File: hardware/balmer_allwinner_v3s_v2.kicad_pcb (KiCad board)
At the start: 4 copper layers, 60 x 60 mm, 118 parts, among them J1 JAE_SIM_Card_SF72S006, J11 Micro_SD_Card_Ebay, J2 UART, J3 Bus_PCI_Express_Mini, J4 USB_C_Receptacle, J8 HR911105_RJ45, SW1 SW_MEC_5G, SW2 SW_MEC_5G, U1 AllwinnerV3S, U10 TLV62568DBV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

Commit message: Small updates
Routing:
- net UART0_RX: track 56.4 -> 59.7 mm
- net UART0_TX: track 52.6 -> 55.0 mm
- net SPI_MISO: track 52.7 -> 53.3 mm

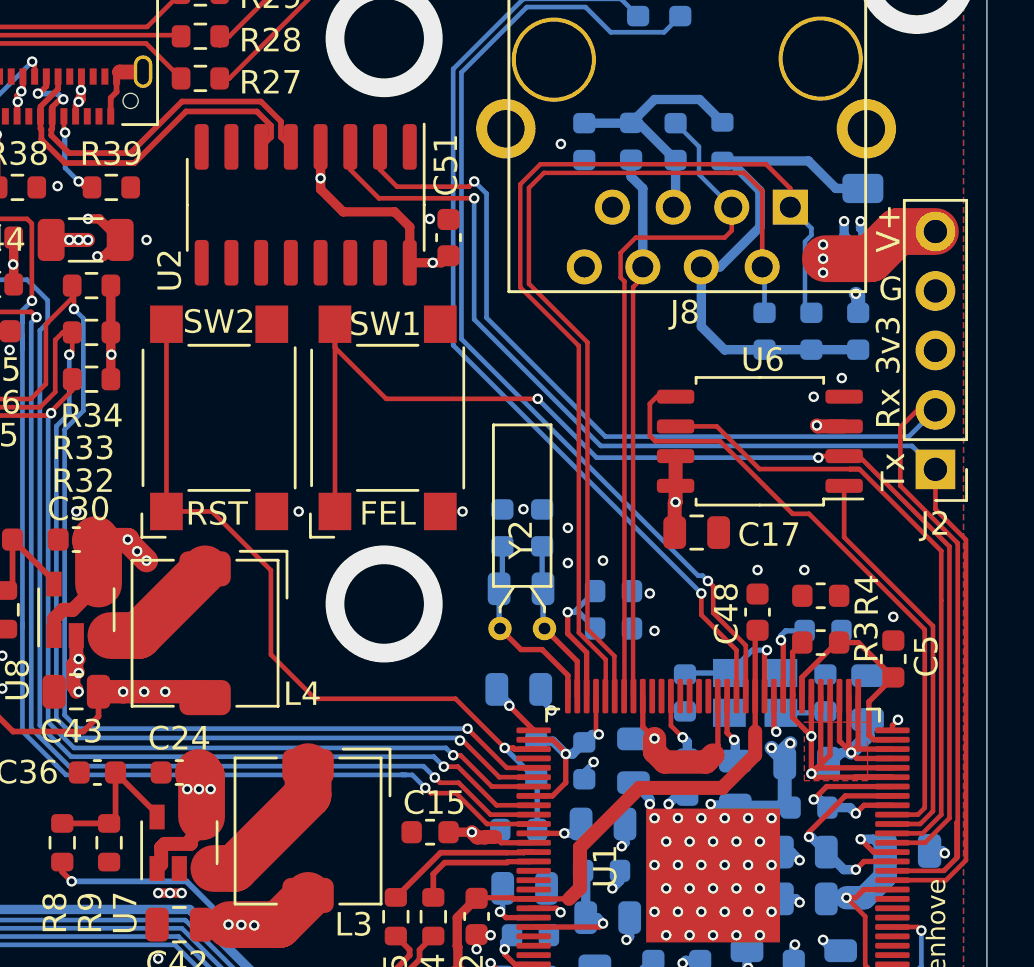
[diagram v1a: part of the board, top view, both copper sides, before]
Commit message: Removed FEL button
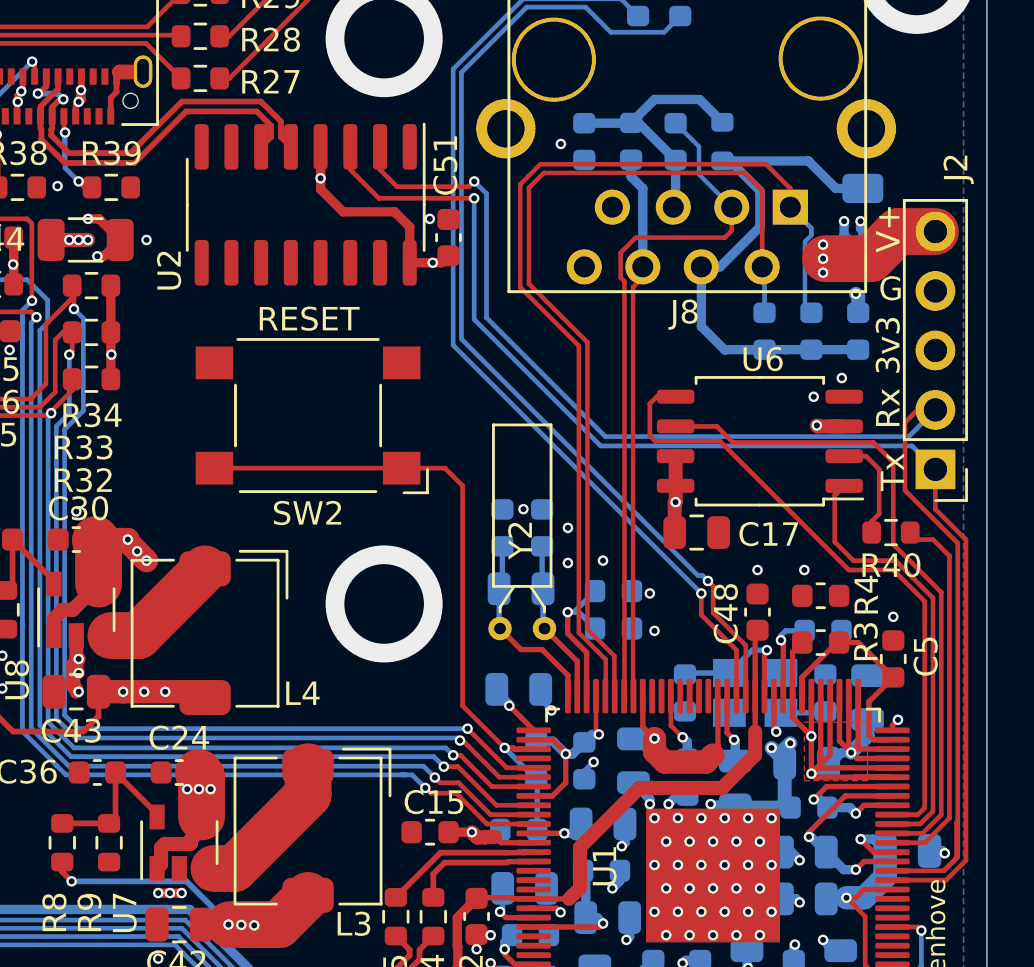
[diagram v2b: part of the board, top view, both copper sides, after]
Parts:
- removed SW1: SW_MEC_5G, Button_Switch_SMD:SW_SPST_Omron_B3FS-100xP
- added R40: 0R, Resistor_SMD:R_0603_1608Metric, F.Cu at (117.9, 101.8)
- moved SW2 3.80 mm to (93.0, 96.8), turned to 180 degrees
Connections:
- U6 pad 2: SPI_MISO -> Net-(R40-Pad2)
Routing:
- net SPI_MISO: track 53.3 -> 16.0 mm, vias 2 -> 0
- net RESET: track 34.1 -> 28.2 mm
- net Net-(R40-Pad2): track 0.00 -> 5.20 mm
- net SPI_CS: track 17.4 -> 18.8 mm
- net SPI_MOSI: track 26.9 -> 27.6 mm
- net SPI_SCK: track 27.6 -> 28.3 mm
- net GND: vias 148 -> 146
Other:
- board text added: "RESET"
- board text removed: "FEL"
- board text removed: "RST"

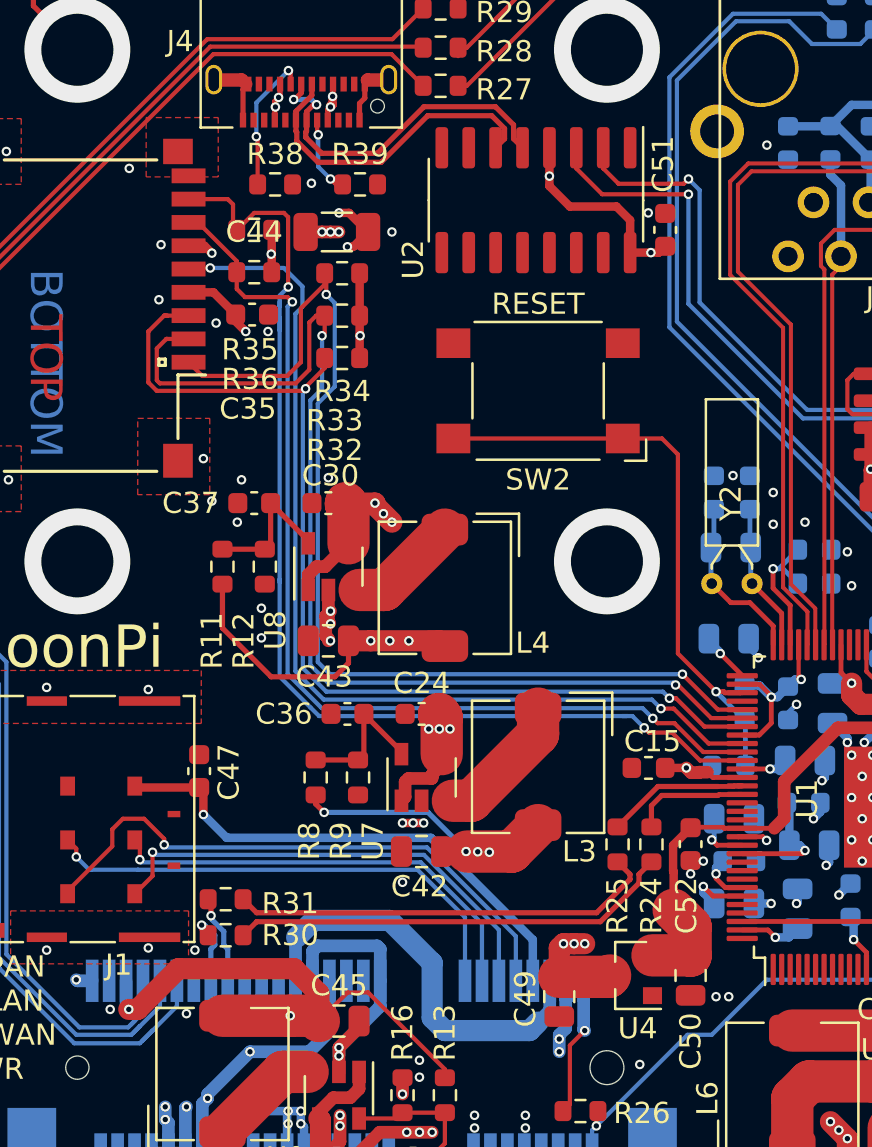
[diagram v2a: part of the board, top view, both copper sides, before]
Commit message: Removed USB series resistors on mPCIe side
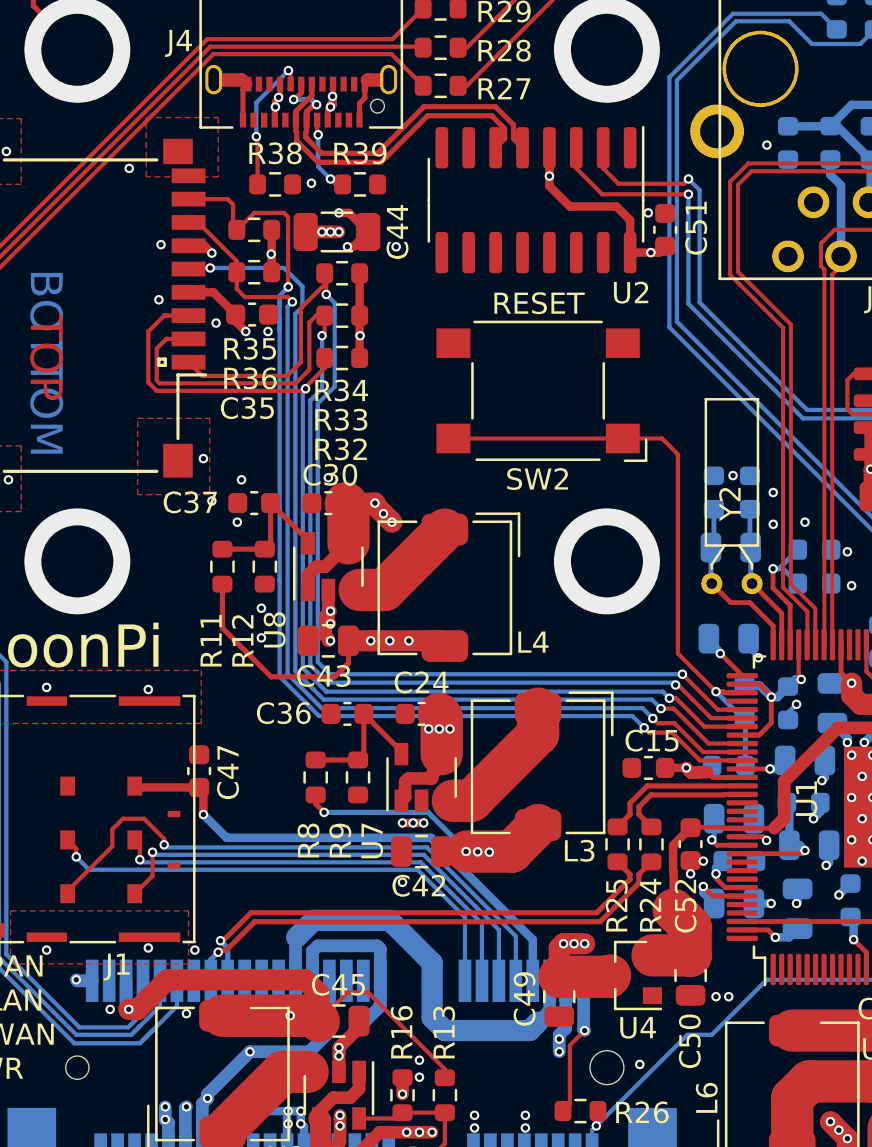
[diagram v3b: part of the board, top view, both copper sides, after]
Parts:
- removed R30, R31: 33, Resistor_SMD:R_0603_1608Metric
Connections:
- J3 pad 36: /Periphery/USB_H-D- -> USB-D-
- J3 pad 38: /Periphery/USB_H-D+ -> USB-D+
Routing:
- net /Periphery/USB_H-D-: track 4.26 -> 0.00 mm, vias 1 -> 0
- net /Periphery/USB_H-D+: track 3.76 -> 0.00 mm, vias 1 -> 0
- net USB-D-: track 20.3 -> 23.6 mm, vias 0 -> 1
- net USB-D+: track 21.0 -> 24.0 mm, vias 0 -> 1
- net /USB_D-D+: track 5.51 -> 6.31 mm

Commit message: Fixed DRC
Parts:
- moved C47 1.10 mm to (78.1, 114.8)
- moved R27 0.60 mm to (89.0, 82.4)
- moved R28 0.60 mm to (89.0, 80.6)
- moved R29 0.60 mm to (89.0, 78.8)
- moved C35 0.50 mm to (79.5, 93.7)
- moved J11 0.50 mm to (66.0, 93.8)
- moved R32 0.50 mm to (83.8, 95.8)
- moved R33 0.50 mm to (83.8, 93.8)
- moved R34 0.50 mm to (83.8, 91.8)
- moved R35 0.50 mm to (79.6, 89.7)
- moved R36 0.50 mm to (79.6, 91.7)
- moved C24 0.40 mm to (87.1, 112.0)
- moved C36 0.40 mm to (83.6, 112.0)
- moved C42 0.40 mm to (87.1, 118.5)
- moved J8 0.40 mm to (108.8, 81.3)
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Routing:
- net GND: track 88.0 -> 93.5 mm
- net VCC: track 176.6 -> 179.2 mm, vias 27 -> 29
- net Net-(C33-Pad1): track 23.8 -> 25.2 mm
- net EPHY-RXP: track 29.7 -> 30.7 mm
- net Net-(J3-Pad44): track 76.0 -> 77.0 mm
- net Net-(C47-Pad1): track 24.4 -> 25.2 mm
- net SDC0_D2: track 50.6 -> 50.0 mm
- net Net-(J3-Pad46): track 71.9 -> 72.5 mm
- net Net-(J3-Pad42): track 76.0 -> 76.6 mm
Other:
- net class Default: clearance 0.1524 -> 0.127
- net class Power: clearance 0.1524 -> 0.127
- rule trace_clearance: 0.1524 -> 0.127
- rule trace_min: 0.1016 -> 0.1778

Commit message: Rotated SIM
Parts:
- moved C47 5.38 mm to (77.9, 120.1), turned to 270 degrees
- moved J1 4.89 mm to (67.3, 115.5), turned to 90 degrees
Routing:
- net GND: track 93.5 -> 122.5 mm, vias 146 -> 139
- net Net-(C47-Pad1): track 25.2 -> 35.5 mm
- net Net-(J1-PadC3): track 22.7 -> 32.9 mm
- net Net-(J1-PadC2): track 21.2 -> 31.0 mm
- net Net-(J1-PadC6): track 23.5 -> 27.2 mm
- net Net-(J1-PadC7): track 27.9 -> 30.3 mm

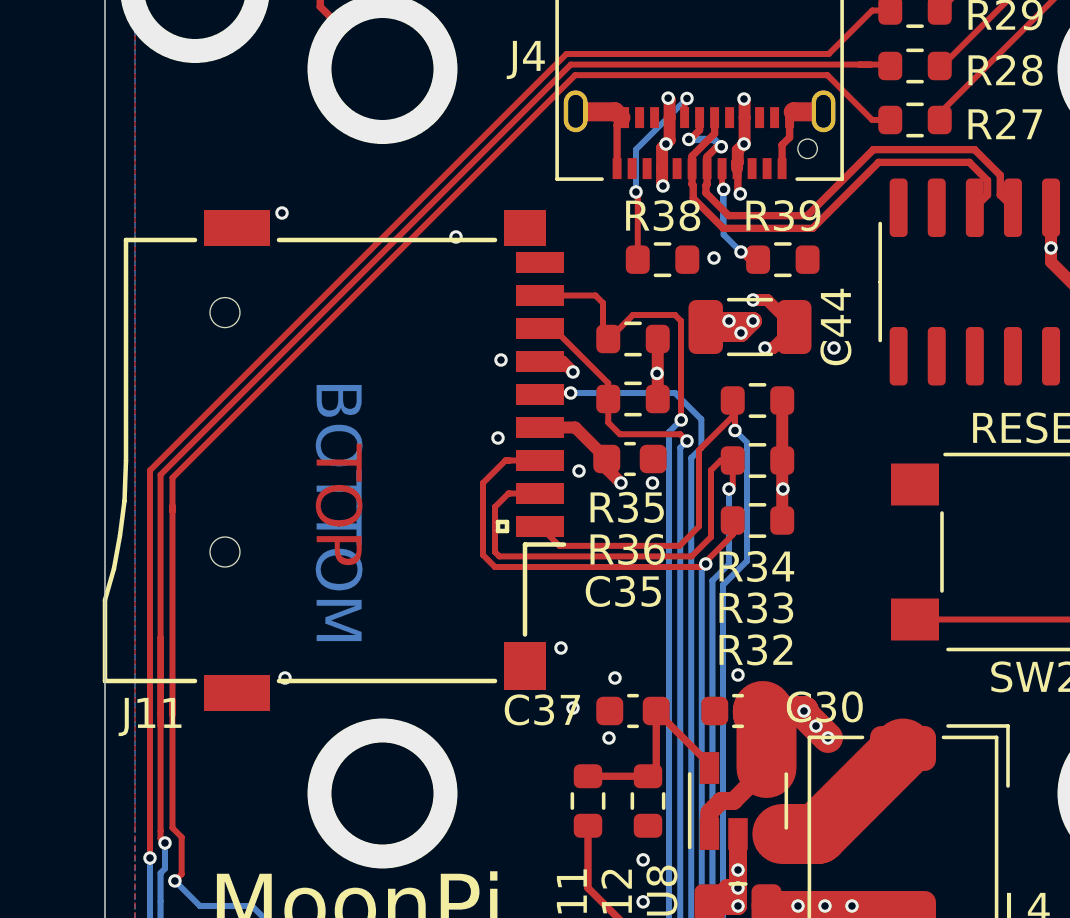
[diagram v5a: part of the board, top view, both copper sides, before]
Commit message: 0R between VBus and VCC
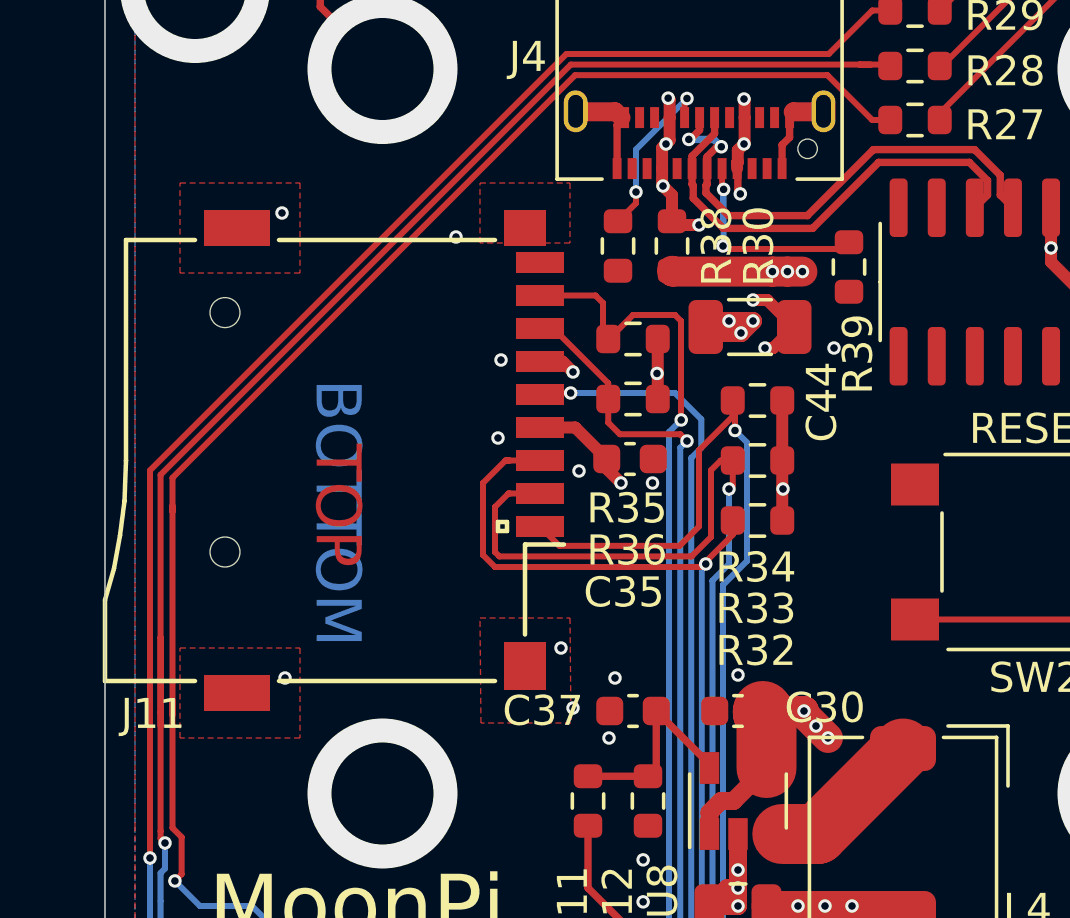
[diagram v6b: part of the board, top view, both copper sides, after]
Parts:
- added R30: 0, Resistor_SMD:R_0603_1608Metric, F.Cu at (80.9, 86.6)
- moved R39 2.22 mm to (86.8, 87.3), turned to 270 degrees
- moved R38 1.55 mm to (79.1, 86.6), turned to 270 degrees
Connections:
- J4 pad A4: VCC -> Net-(J4-PadA4)
- J4 pad A9: VCC -> Net-(J4-PadA4)
- J4 pad B4: VCC -> Net-(J4-PadA4)
- J4 pad B9: VCC -> Net-(J4-PadA4)
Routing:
- net VCC: track 179.2 -> 196.0 mm, vias 29 -> 26
- net Net-(J4-PadA4): track 0.00 -> 10.6 mm, vias 0 -> 7
- net Net-(J4-PadA5): track 5.01 -> 8.24 mm
- net Net-(J4-PadB5): track 6.77 -> 5.80 mm
- net GND: vias 139 -> 138

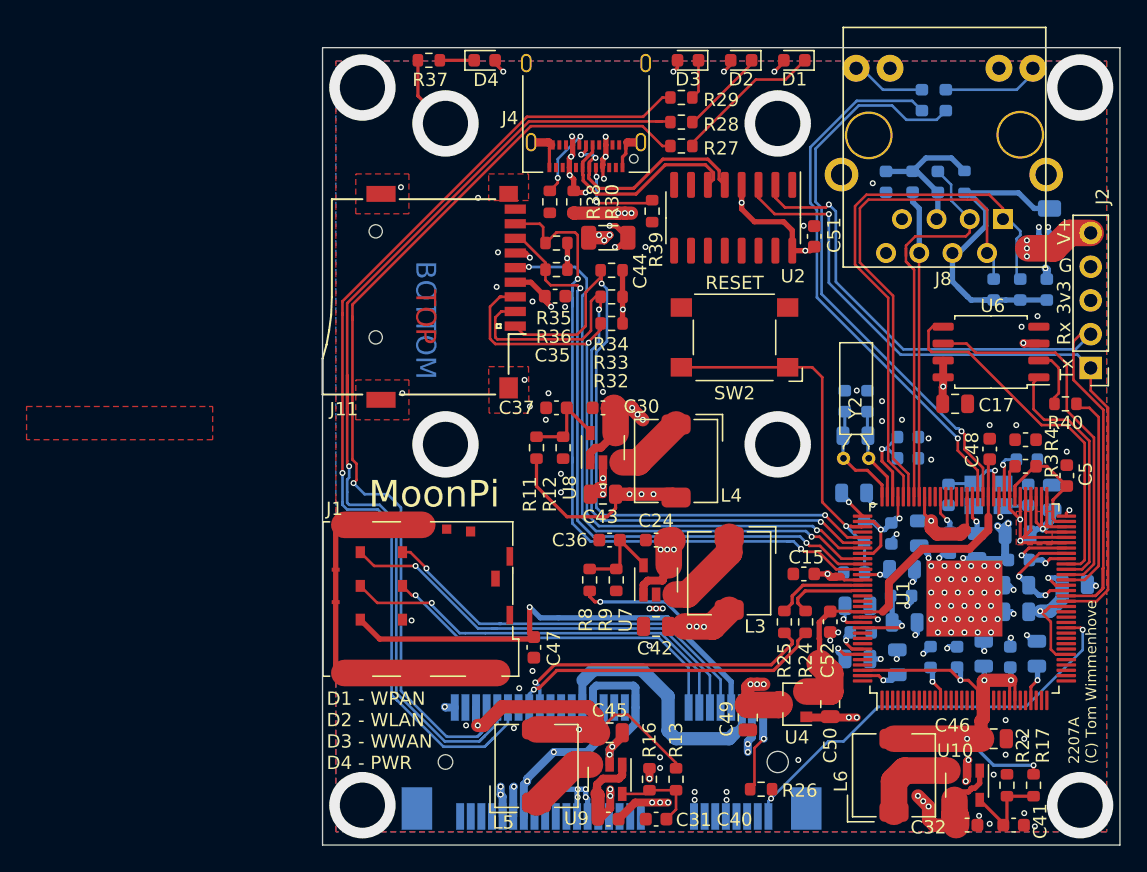
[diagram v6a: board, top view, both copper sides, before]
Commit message: Added an "RDY" LED
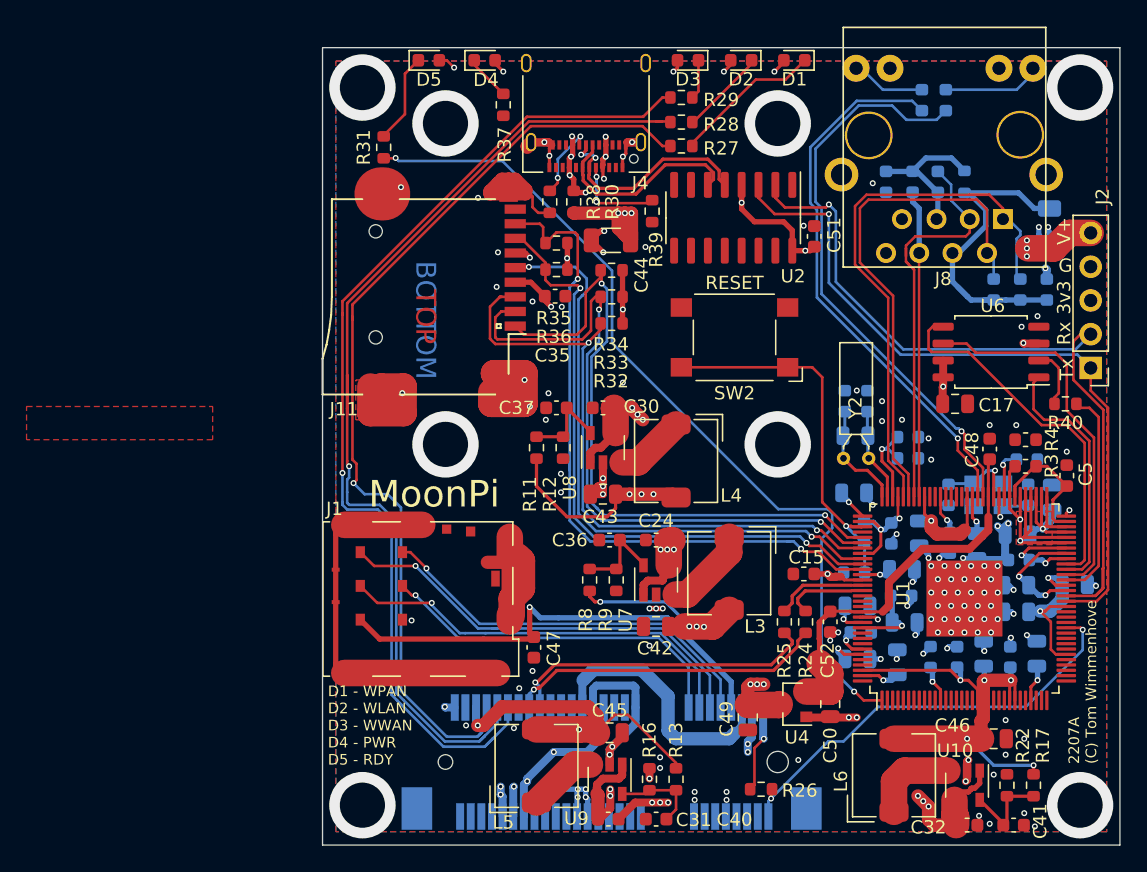
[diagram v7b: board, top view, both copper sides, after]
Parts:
- added D5: LED, LED_SMD:LED_0603_1608Metric, F.Cu at (70.0, 76.0)
- added R31: 200R, Resistor_SMD:R_0603_1608Metric, F.Cu at (66.6, 82.5)
- R37: value 1k -> 220
- moved R37 6.53 mm to (75.6, 79.3), turned to 90 degrees
- moved C44 0.28 mm to (83.7, 89.5), turned to 180 degrees
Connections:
- D4 pad 2: VCC -> +3V3
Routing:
- net SDC1_D2: track 0.00 -> 65.1 mm, vias 0 -> 2
- net GND: track 122.5 -> 160.9 mm, vias 138 -> 141
- net Net-(D5-Pad1): track 0.00 -> 6.81 mm
- net VCC: track 196.0 -> 191.2 mm, vias 26 -> 23
- net +3V3: track 168.0 -> 170.5 mm, vias 30 -> 32
- net Net-(D4-Pad1): track 2.59 -> 3.43 mm
- net SDC0_D1: track 52.8 -> 53.5 mm
- removed copper zone on In2.Cu, net VCC
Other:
- board text added: "D1 - WPAN D2 - WLAN D3 - WWAN D4 - PWR D5 - RDY"
- board text removed: "D1 - WPAN D2 - WLAN D3 - WWAN D4 - PWR"
